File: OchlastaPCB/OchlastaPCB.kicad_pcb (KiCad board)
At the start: 4 copper layers, 175.1 x 89.9 mm, 37 parts, among them J1 XT60PW-M, J2 5V, U1 AP64501SP-13, U2 AP3429, U3 STM32F334R8Tx

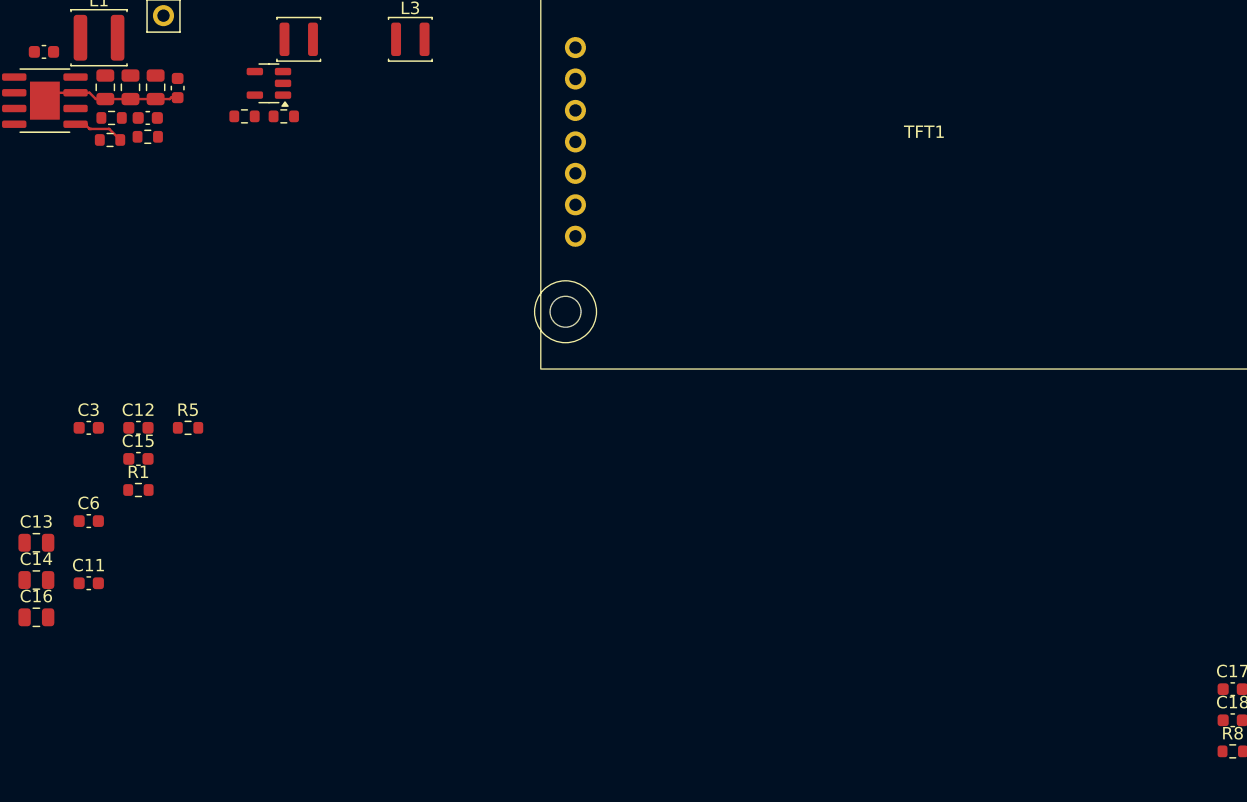
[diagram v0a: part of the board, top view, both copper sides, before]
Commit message: Precision LDO for analog circuitry in schematics
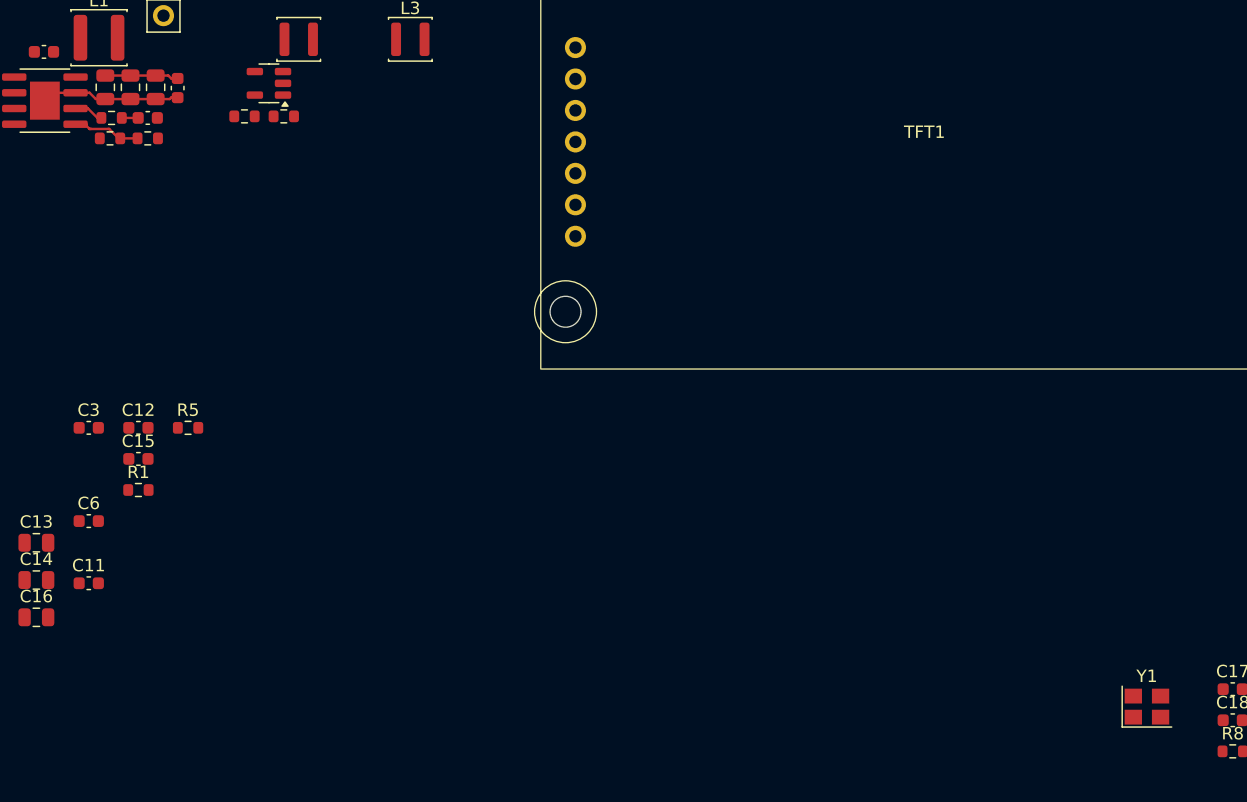
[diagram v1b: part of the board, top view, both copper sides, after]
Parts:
- added Y1: Crystal_GND24, Crystal:Crystal_SMD_3225-4Pin_3.2x2.5mm, F.Cu at (171.5, 94.0)
- moved R3 0.13 mm to (90.8, 48.1)
- moved R4 0.13 mm to (87.8, 48.1)
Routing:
- net 5V: track 0.00 -> 5.94 mm
- net Net-(U1-COMP): track 0.00 -> 2.40 mm
- net Net-(U1-FB): track 4.34 -> 5.74 mm
- net Net-(C5-Pad1): track 0.00 -> 1.32 mm

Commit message: Schematics seems finished, starting PCB design
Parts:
- added C19: 10n, Capacitor_SMD:C_0603_1608Metric, F.Cu at (395.9, 108.9)
- added C20: 100 nF, Capacitor_SMD:C_0603_1608Metric, F.Cu at (395.9, 111.4)
- added C21: 22 uF, Capacitor_SMD:C_0805_2012Metric, F.Cu at (485.3, 58.2)
- added C22: 100 n, Capacitor_SMD:C_0603_1608Metric, F.Cu at (395.9, 113.9)
- added C23: 100 n, Capacitor_SMD:C_0603_1608Metric, F.Cu at (395.9, 116.4)
- added C24: 100 n, Capacitor_SMD:C_0603_1608Metric, F.Cu at (399.9, 81.3)
- added C25: 100 n, Capacitor_SMD:C_0603_1608Metric, F.Cu at (399.9, 83.8)
- added C26: 100 n, Capacitor_SMD:C_0603_1608Metric, F.Cu at (399.9, 86.3)
- added C27: 100 n, Capacitor_SMD:C_0603_1608Metric, F.Cu at (399.9, 88.8)
- added C28: 100 n, Capacitor_SMD:C_0603_1608Metric, F.Cu at (399.9, 91.3)
- added C29: 10 uF 50V, Capacitor_SMD:C_1206_3216Metric, F.Cu at (85.0, 122.4)
- added C30: 10 uF 50V, Capacitor_SMD:C_1206_3216Metric, F.Cu at (85.0, 125.8)
- added C31: 10 nF, Capacitor_SMD:C_0603_1608Metric, F.Cu at (399.9, 93.8)
- added C32: 100 nF, Capacitor_SMD:C_0603_1608Metric, F.Cu at (399.9, 96.3)
- added C33: 2.7 nF, Capacitor_SMD:C_0603_1608Metric, F.Cu at (399.9, 98.8)
- added C34: open, Capacitor_SMD:C_0603_1608Metric, F.Cu at (399.9, 101.3)
- added C35: 100 nF, Capacitor_SMD:C_0603_1608Metric, F.Cu at (399.9, 103.9)
- added C36: 22 uF, Capacitor_SMD:C_0805_2012Metric, F.Cu at (485.3, 61.2)
- added C37: 22 uF, Capacitor_SMD:C_0805_2012Metric, F.Cu at (485.3, 64.2)
- added C38: 100 n, Capacitor_SMD:C_0603_1608Metric, F.Cu at (399.9, 106.4)
- added C39: 1 u, Capacitor_SMD:C_0603_1608Metric, F.Cu at (399.9, 108.9)
- added C40: 100 n, Capacitor_SMD:C_0603_1608Metric, F.Cu at (399.9, 111.4)
- added C41: 10 uF 50V, Capacitor_SMD:C_1206_3216Metric, F.Cu at (396.7, 169.3)
- added C42: 10 uF 50V, Capacitor_SMD:C_1206_3216Metric, F.Cu at (402.4, 155.9)
- added C43: 10 uF 50V, Capacitor_SMD:C_1206_3216Metric, F.Cu at (402.4, 159.2)
- added C44: 10 uF 50V, Capacitor_SMD:C_1206_3216Metric, F.Cu at (402.4, 162.6)
- added C45: 100 n, Capacitor_SMD:C_0603_1608Metric, F.Cu at (399.9, 113.9)
- added C46: 1 u, Capacitor_SMD:C_0603_1608Metric, F.Cu at (399.9, 116.4)
- added C47: 100 n, Capacitor_SMD:C_0603_1608Metric, F.Cu at (403.9, 81.3)
- added C48: 10 uF 50V, Capacitor_SMD:C_1206_3216Metric, F.Cu at (402.4, 165.9)
- added C49: 10 uF 50V, Capacitor_SMD:C_1206_3216Metric, F.Cu at (402.4, 169.3)
- added C50: 10 uF 50V, Capacitor_SMD:C_1206_3216Metric, F.Cu at (408.0, 155.9)
- added C51: 10 uF 50V, Capacitor_SMD:C_1206_3216Metric, F.Cu at (408.0, 159.2)
- added C52: 100 n, Capacitor_SMD:C_0603_1608Metric, F.Cu at (403.9, 83.8)
- added C53: 100 n, Capacitor_SMD:C_0603_1608Metric, F.Cu at (403.9, 86.3)
- added C54: 1 u, Capacitor_SMD:C_0603_1608Metric, F.Cu at (403.9, 88.8)
- added C55: 1 u, Capacitor_SMD:C_0603_1608Metric, F.Cu at (403.9, 91.3)
- added C56: 100 n, Capacitor_SMD:C_0603_1608Metric, F.Cu at (403.9, 93.8)
- added C57: 100 n, Capacitor_SMD:C_0603_1608Metric, F.Cu at (403.9, 96.3)
- added C58: 10 uF 50V, Capacitor_SMD:C_1206_3216Metric, F.Cu at (408.0, 162.6)
- added C59: 10 uF 50V, Capacitor_SMD:C_1206_3216Metric, F.Cu at (408.0, 165.9)
- added C60: 10 uF 50V, Capacitor_SMD:C_1206_3216Metric, F.Cu at (408.0, 169.3)
- added C61: 10 uF 50V, Capacitor_SMD:C_1206_3216Metric, F.Cu at (413.7, 155.9)
- added C62: 10 uF 50V, Capacitor_SMD:C_1206_3216Metric, F.Cu at (413.7, 159.2)
- added C63: 10 uF 50V, Capacitor_SMD:C_1206_3216Metric, F.Cu at (413.7, 162.6)
- added C64: 10 uF 50V, Capacitor_SMD:C_1206_3216Metric, F.Cu at (413.7, 165.9)
- added C65: 10 uF 50V, Capacitor_SMD:C_1206_3216Metric, F.Cu at (413.7, 169.3)
- added C66: 100 n, Capacitor_SMD:C_0603_1608Metric, F.Cu at (403.9, 98.8)
- added C67: 100 n, Capacitor_SMD:C_0603_1608Metric, F.Cu at (403.9, 101.3)
- added C68: 100 n, Capacitor_SMD:C_0603_1608Metric, F.Cu at (403.9, 103.9)
- added C69: 100 n, Capacitor_SMD:C_0603_1608Metric, F.Cu at (403.9, 106.4)
- added C70: 100 n, Capacitor_SMD:C_0603_1608Metric, F.Cu at (403.9, 108.9)
- added C71: 100 n, Capacitor_SMD:C_0603_1608Metric, F.Cu at (403.9, 111.4)
- added C72: 100 n, Capacitor_SMD:C_0603_1608Metric, F.Cu at (403.9, 113.9)
- added C73: 100 n, Capacitor_SMD:C_0603_1608Metric, F.Cu at (403.9, 116.4)
- added C74: 100 n, Capacitor_SMD:C_0603_1608Metric, F.Cu at (408.0, 81.3)
- added C75: 100 n, Capacitor_SMD:C_0603_1608Metric, F.Cu at (408.0, 83.8)
- added CP2: 100 uF, Capacitor_SMD:CP_Elec_8x10, F.Cu at (69.4, 57.4)
- added CP3: 100 uF, Capacitor_SMD:CP_Elec_8x10, F.Cu at (436.1, 120.9)
- added CP4: 100 uF, Capacitor_SMD:CP_Elec_8x10, F.Cu at (436.1, 130.8)
- added CP5: 100 uF, Capacitor_SMD:CP_Elec_8x10, F.Cu at (436.1, 140.6)
- added CP6: 100 uF, Capacitor_SMD:CP_Elec_8x10, F.Cu at (436.1, 150.5)
- added D1: SS14, Diode_SMD:D_SMA, F.Cu at (445.9, 98.6)
- added D10: SS14, Diode_SMD:D_SMA, F.Cu at (454.0, 112.2)
- added D11: SS14, Diode_SMD:D_SMA, F.Cu at (454.0, 116.8)
- added D12: SS14, Diode_SMD:D_SMA, F.Cu at (454.0, 121.3)
- added D13: SS14, Diode_SMD:D_SMA, F.Cu at (462.1, 98.6)
- added D14: SS14, Diode_SMD:D_SMA, F.Cu at (462.1, 103.1)
- added D15: SS14, Diode_SMD:D_SMA, F.Cu at (462.1, 107.7)
- added D16: SS14, Diode_SMD:D_SMA, F.Cu at (462.1, 112.2)
- added D2: SS14, Diode_SMD:D_SMA, F.Cu at (445.9, 103.1)
- added D3: SS14, Diode_SMD:D_SMA, F.Cu at (445.9, 107.7)
- added D4: SS14, Diode_SMD:D_SMA, F.Cu at (445.9, 112.2)
- added D5: SS14, Diode_SMD:D_SMA, F.Cu at (445.9, 116.8)
- added D6: SS14, Diode_SMD:D_SMA, F.Cu at (445.9, 121.3)
- added D7: SS14, Diode_SMD:D_SMA, F.Cu at (454.0, 98.6)
- added D8: SS14, Diode_SMD:D_SMA, F.Cu at (454.0, 103.1)
- added D9: SS14, Diode_SMD:D_SMA, F.Cu at (454.0, 107.7)
- added H1: MountingHole_Pad, MountingHole:MountingHole_3.2mm_M3_Pad_Via, F.Cu at (470.1, 45.6)
- added H2: MountingHole_Pad, MountingHole:MountingHole_3.2mm_M3_Pad_Via, F.Cu at (470.1, 53.6)
- added H3: MountingHole_Pad, MountingHole:MountingHole_3.2mm_M3_Pad_Via, F.Cu at (470.1, 61.5)
- added H4: MountingHole_Pad, MountingHole:MountingHole_3.2mm_M3_Pad_Via, F.Cu at (470.1, 69.5)
- added J10: CAN term jmp, Connector_PinHeader_2.54mm:PinHeader_1x02_P2.54mm_Vertical, F.Cu at (481.0, 69.8)
- added J3: Conn_01x02_Socket, TerminalBlock_WAGO:TerminalBlock_WAGO_236-402_1x02_P5.00mm_45Degree, F.Cu at (38.5, 76.3)
- added J4: Conn_01x02_Socket, TerminalBlock_WAGO:TerminalBlock_WAGO_236-402_1x02_P5.00mm_45Degree, F.Cu at (38.5, 90.0)
- added J5: Conn_01x02_Socket, TerminalBlock_WAGO:TerminalBlock_WAGO_236-402_1x02_P5.00mm_45Degree, F.Cu at (38.5, 103.7)
- added J6: Conn_01x02_Socket, TerminalBlock_WAGO:TerminalBlock_WAGO_236-402_1x02_P5.00mm_45Degree, F.Cu at (38.5, 117.5)
- added J7: Debug, Connector_IDC:IDC-Header_2x05_P2.54mm_Vertical, F.Cu at (121.9, 19.6)
- added J8: UART, Connector_PinHeader_2.54mm:PinHeader_1x03_P2.54mm_Vertical, F.Cu at (418.8, 165.4)
- added J9: CAN, Connector_Phoenix_MC:PhoenixContact_MC_1,5_2-G-3.81_1x02_P3.81mm_Horizontal, F.Cu at (97.4, 25.8)
- added L4: 3.6 uH, Inductor_SMD:L_Changjiang_FNR4030S, F.Cu at (457.0, 72.5)
- added L5: 22 uH, Inductor_SMD:L_APV_APH1770, F.Cu at (384.0, 108.2)
- added L6: 22 uH, Inductor_SMD:L_APV_APH1770, F.Cu at (384.0, 127.0)
- added L7: 22 uH, Inductor_SMD:L_APV_APH1770, F.Cu at (384.0, 145.8)
- added Q1: IRFH7440, SnapMagic_downloads:PQFN_5x6_FET, F.Cu at (446.3, 126.9)
- added Q2: IRFH7440, SnapMagic_downloads:PQFN_5x6_FET, F.Cu at (446.3, 133.6)
- added Q3: IRFH7440, SnapMagic_downloads:PQFN_5x6_FET, F.Cu at (446.3, 140.2)
- added Q4: IRFH7440, SnapMagic_downloads:PQFN_5x6_FET, F.Cu at (446.3, 146.9)
- added Q5: IRFH7440, SnapMagic_downloads:PQFN_5x6_FET, F.Cu at (446.3, 153.5)
- added Q6: IRFH7440, SnapMagic_downloads:PQFN_5x6_FET, F.Cu at (454.9, 126.9)
- added Q7: IRFH7440, SnapMagic_downloads:PQFN_5x6_FET, F.Cu at (454.9, 133.6)
- added Q8: IRFH7440, SnapMagic_downloads:PQFN_5x6_FET, F.Cu at (454.9, 140.2)
- added R10: 40 k 1%, Resistor_SMD:R_0603_1608Metric, F.Cu at (408.0, 108.9)
- added R11: 22.1 k 1%, Resistor_SMD:R_0603_1608Metric, F.Cu at (408.0, 111.4)
- added R12: 10 k, Resistor_SMD:R_0603_1608Metric, F.Cu at (408.0, 113.9)
- added R13: 15 k, Resistor_SMD:R_0603_1608Metric, F.Cu at (408.0, 116.4)
- added R14: 200k 1%, Resistor_SMD:R_0603_1608Metric, F.Cu at (412.0, 81.3)
- added R15: 22.1 k 1%, Resistor_SMD:R_0603_1608Metric, F.Cu at (412.0, 83.8)
- added R16: 10 R, Resistor_SMD:R_0603_1608Metric, F.Cu at (412.0, 86.3)
- added R17: 10 R, Resistor_SMD:R_0603_1608Metric, F.Cu at (412.0, 88.8)
- added R18: 10 R, Resistor_SMD:R_0603_1608Metric, F.Cu at (412.0, 91.3)
- added R19: 10 R, Resistor_SMD:R_0603_1608Metric, F.Cu at (412.0, 93.8)
- added R20: 10 R, Resistor_SMD:R_0603_1608Metric, F.Cu at (412.0, 96.3)
- added R21: 10 R, Resistor_SMD:R_0603_1608Metric, F.Cu at (412.0, 98.8)
- added R22: 10 R, Resistor_SMD:R_0603_1608Metric, F.Cu at (412.0, 101.3)
- added R23: 10 R, Resistor_SMD:R_0603_1608Metric, F.Cu at (412.0, 103.9)
- added R24: 10 R, Resistor_SMD:R_0603_1608Metric, F.Cu at (412.0, 106.4)
- added R25: 10 R, Resistor_SMD:R_0603_1608Metric, F.Cu at (412.0, 108.9)
- added R26: 10 R, Resistor_SMD:R_0603_1608Metric, F.Cu at (412.0, 111.4)
- added R27: 10 R, Resistor_SMD:R_0603_1608Metric, F.Cu at (412.0, 113.9)
- added R28: 10 R, Resistor_SMD:R_0603_1608Metric, F.Cu at (412.0, 116.4)
- added R29: 10 R, Resistor_SMD:R_0603_1608Metric, F.Cu at (416.0, 81.3)
- added R30: 10 R, Resistor_SMD:R_0603_1608Metric, F.Cu at (416.0, 83.8)
- added R31: 10 R, Resistor_SMD:R_0603_1608Metric, F.Cu at (416.0, 86.3)
- added R32: 10k, Resistor_SMD:R_0603_1608Metric, F.Cu at (416.0, 88.8)
- added R33: 10k, Resistor_SMD:R_0603_1608Metric, F.Cu at (416.0, 91.3)
- added R34: 200k 1%, Resistor_SMD:R_0603_1608Metric, F.Cu at (59.2, 71.1)
- added R35: 22.1 k 1%, Resistor_SMD:R_0603_1608Metric, F.Cu at (416.0, 96.3)
- added R36: 200k 1%, Resistor_SMD:R_0603_1608Metric, F.Cu at (416.0, 98.8)
- added R37: 22.1 k 1%, Resistor_SMD:R_0603_1608Metric, F.Cu at (416.0, 101.3)
- added R38: 200k 1%, Resistor_SMD:R_0603_1608Metric, F.Cu at (416.0, 103.9)
- added R39: 22.1 k 1%, Resistor_SMD:R_0603_1608Metric, F.Cu at (416.0, 106.4)
- added R40: 200k 1%, Resistor_SMD:R_0603_1608Metric, F.Cu at (416.0, 108.9)
- added R41: 22.1 k 1%, Resistor_SMD:R_0603_1608Metric, F.Cu at (416.0, 111.4)
- added R42: 200k 1%, Resistor_SMD:R_0603_1608Metric, F.Cu at (416.0, 113.9)
- added R43: 22.1 k 1%, Resistor_SMD:R_0603_1608Metric, F.Cu at (416.0, 116.4)
- added R44: 120 R, Resistor_SMD:R_0603_1608Metric, F.Cu at (420.0, 81.3)
- added R45: 120 R / DNP, Resistor_SMD:R_0603_1608Metric, F.Cu at (420.0, 83.8)
- added R46: DNP / 120 R, Resistor_SMD:R_0603_1608Metric, F.Cu at (420.0, 86.3)
- added R47: 10 k, Resistor_SMD:R_0603_1608Metric, F.Cu at (420.0, 88.8)
- added R48: 10 k, Resistor_SMD:R_0603_1608Metric, F.Cu at (420.0, 91.3)
- added R49: 10 k, Resistor_SMD:R_0603_1608Metric, F.Cu at (420.0, 93.8)
- added R50: 10 k, Resistor_SMD:R_0603_1608Metric, F.Cu at (420.0, 96.3)
- added R51: 10 k, Resistor_SMD:R_0603_1608Metric, F.Cu at (420.0, 98.8)
- added R52: 10 k, Resistor_SMD:R_0603_1608Metric, F.Cu at (420.0, 101.3)
- added R53: 10 k, Resistor_SMD:R_0603_1608Metric, F.Cu at (420.0, 103.9)
- added R54: 10 k, Resistor_SMD:R_0603_1608Metric, F.Cu at (420.0, 106.4)
- added R55: 10 k, Resistor_SMD:R_0603_1608Metric, F.Cu at (420.0, 108.9)
- added R9: 10 k, Resistor_SMD:R_0603_1608Metric, F.Cu at (408.0, 106.4)
- added Ra1: 22.1 k 1%, Resistor_SMD:R_0603_1608Metric, F.Cu at (420.0, 111.4)
- added Ra2: 22.1 k 1%, Resistor_SMD:R_0603_1608Metric, F.Cu at (420.0, 113.9)
- added Ra3: 22.1 k 1%, Resistor_SMD:R_0603_1608Metric, F.Cu at (420.0, 116.4)
- added Ra4: 22.1 k 1%, Resistor_SMD:R_0603_1608Metric, F.Cu at (424.0, 81.3)
- added Ra5: 22.1 k 1%, Resistor_SMD:R_0603_1608Metric, F.Cu at (424.0, 83.8)
- added Ra6: 22.1 k 1%, Resistor_SMD:R_0603_1608Metric, F.Cu at (424.0, 86.3)
- added Ra7: 22.1 k 1%, Resistor_SMD:R_0603_1608Metric, F.Cu at (424.0, 88.8)
- added Ra8: 22.1 k 1%, Resistor_SMD:R_0603_1608Metric, F.Cu at (424.0, 91.3)
- added Rb1: 22.1 k 1%, Resistor_SMD:R_0603_1608Metric, F.Cu at (424.0, 93.8)
- added Rb2: 22.1 k 1%, Resistor_SMD:R_0603_1608Metric, F.Cu at (424.0, 96.3)
- added Rb3: 22.1 k 1%, Resistor_SMD:R_0603_1608Metric, F.Cu at (424.0, 98.8)
- added Rb4: 22.1 k 1%, Resistor_SMD:R_0603_1608Metric, F.Cu at (424.0, 101.3)
- added Rb5: 22.1 k 1%, Resistor_SMD:R_0603_1608Metric, F.Cu at (424.0, 103.9)
- added Rb6: 22.1 k 1%, Resistor_SMD:R_0603_1608Metric, F.Cu at (424.0, 106.4)
- added Rb7: 22.1 k 1%, Resistor_SMD:R_0603_1608Metric, F.Cu at (424.0, 108.9)
- added Rb8: 22.1 k 1%, Resistor_SMD:R_0603_1608Metric, F.Cu at (424.0, 111.4)
- added Rc1: 820 R, Resistor_SMD:R_0603_1608Metric, F.Cu at (424.0, 113.9)
- added Rc2: 820 R, Resistor_SMD:R_0603_1608Metric, F.Cu at (424.0, 116.4)
- added Rc3: 820 R, Resistor_SMD:R_0603_1608Metric, F.Cu at (428.0, 81.3)
- added Rc4: 820 R, Resistor_SMD:R_0603_1608Metric, F.Cu at (428.0, 83.8)
- added Rc5: 820 R, Resistor_SMD:R_0603_1608Metric, F.Cu at (428.0, 86.3)
- added Rc6: 820 R, Resistor_SMD:R_0603_1608Metric, F.Cu at (428.0, 88.8)
- added Rc7: 820 R, Resistor_SMD:R_0603_1608Metric, F.Cu at (428.0, 91.3)
- added Rc8: 820 R, Resistor_SMD:R_0603_1608Metric, F.Cu at (428.0, 93.8)
- added Rg1: 2.7 k 1%, Resistor_SMD:R_0603_1608Metric, F.Cu at (428.0, 96.3)
- added Rg2: 2.7 k 1%, Resistor_SMD:R_0603_1608Metric, F.Cu at (428.0, 98.8)
- added Rg3: 2.7 k 1%, Resistor_SMD:R_0603_1608Metric, F.Cu at (428.0, 101.3)
- added Rg4: 2.7 k 1%, Resistor_SMD:R_0603_1608Metric, F.Cu at (428.0, 103.9)
- added Rg5: 2.7 k 1%, Resistor_SMD:R_0603_1608Metric, F.Cu at (428.0, 106.4)
- added Rg6: 2.7 k 1%, Resistor_SMD:R_0603_1608Metric, F.Cu at (428.0, 108.9)
- added Rg7: 2.7 k 1%, Resistor_SMD:R_0603_1608Metric, F.Cu at (428.0, 111.4)
- added Rg8: 2.7 k 1%, Resistor_SMD:R_0603_1608Metric, F.Cu at (428.0, 113.9)
- added Rshunt1: 5 mR, Resistor_SMD:R_1206_3216Metric, F.Cu at (64.5, 80.3)
- added Rshunt2: 5 mR, Resistor_SMD:R_1206_3216Metric, F.Cu at (481.7, 166.1)
- added Rshunt3: 5 mR, Resistor_SMD:R_1206_3216Metric, F.Cu at (481.7, 169.4)
- added Rshunt4: 5 mR, Resistor_SMD:R_1206_3216Metric, F.Cu at (481.7, 172.7)
- added SW1: SW_RESET, OchlastaFootprints:SW_Push_SPST_CheapAtJLC, F.Cu at (419.8, 156.4)
- added SW2: SW_BOOT, OchlastaFootprints:SW_Push_SPST_CheapAtJLC, F.Cu at (419.8, 160.9)
- added SW3: BTN_A, Button_Switch_THT:SW_PUSH_6mm, F.Cu at (461.0, 125.6)
- added SW4: RotaryEncoder_Switch, Rotary_Encoder:RotaryEncoder_Alps_EC11E-Switch_Vertical_H20mm, F.Cu at (468.1, 101.4)
- added SW5: BTN_B, Button_Switch_THT:SW_PUSH_6mm, F.Cu at (461.0, 134.2)
- added SW6: BTN_C, Button_Switch_THT:SW_PUSH_6mm, F.Cu at (461.0, 142.7)
- added SW7: BTN_D, Button_Switch_THT:SW_PUSH_6mm, F.Cu at (461.0, 151.3)
- added SW8: BTN_L, Button_Switch_THT:SW_PUSH_6mm, F.Cu at (461.0, 159.8)
- added SW9: BTN_R, Button_Switch_THT:SW_PUSH_6mm, F.Cu at (461.0, 168.4)
- added TH1: PT1000, Connector_Phoenix_MC:PhoenixContact_MC_1,5_2-G-3.81_1x02_P3.81mm_Horizontal, F.Cu at (223.1, 53.7)
- added TH2: PT1000, Connector_Phoenix_MC:PhoenixContact_MC_1,5_2-G-3.81_1x02_P3.81mm_Horizontal, F.Cu at (223.1, 63.8)
- added TH3: PT1000, Connector_Phoenix_MC:PhoenixContact_MC_1,5_2-G-3.81_1x02_P3.81mm_Horizontal, F.Cu at (223.1, 74.0)
- added TH4: PT1000, Connector_Phoenix_MC:PhoenixContact_MC_1,5_2-G-3.81_1x02_P3.81mm_Horizontal, F.Cu at (223.1, 84.1)
- added TH5: PT1000, Connector_Phoenix_MC:PhoenixContact_MC_1,5_2-G-3.81_1x02_P3.81mm_Horizontal, F.Cu at (223.1, 94.3)
- added TH6: PT1000, Connector_Phoenix_MC:PhoenixContact_MC_1,5_2-G-3.81_1x02_P3.81mm_Horizontal, F.Cu at (223.1, 104.5)
- added TH7: PT1000, Connector_Phoenix_MC:PhoenixContact_MC_1,5_2-G-3.81_1x02_P3.81mm_Horizontal, F.Cu at (223.1, 114.6)
- added TH8: PT1000, Connector_Phoenix_MC:PhoenixContact_MC_1,5_2-G-3.81_1x02_P3.81mm_Horizontal, F.Cu at (223.1, 124.8)
- added U10: INA333xxDGK, Package_SO:VSSOP-8_3x3mm_P0.65mm, F.Cu at (450.4, 67.3)
- added U11: INA333xxDGK, Package_SO:VSSOP-8_3x3mm_P0.65mm, F.Cu at (450.4, 71.9)
- added U12: INA333xxDGK, Package_SO:VSSOP-8_3x3mm_P0.65mm, F.Cu at (450.4, 76.6)
- added U13: UCC27282DR, SnapMagic_downloads:SOIC127P599X175-8N, F.Cu at (478.9, 44.9)
- added U14: AP64501SP-13, SnapMagic_downloads:SOIC127P600X170-9N, F.Cu at (474.7, 171.2)
- added U15: UCC27282DR, SnapMagic_downloads:SOIC127P599X175-8N, F.Cu at (478.9, 51.3)
- added U16: UCC27282DR, SnapMagic_downloads:SOIC127P599X175-8N, F.Cu at (478.9, 57.8)
- added U17: UCC27282DR, SnapMagic_downloads:SOIC127P599X175-8N, F.Cu at (478.9, 64.3)
- added U18: INA240A2D, Package_SO:SOIC-8_3.9x4.9mm_P1.27mm, F.Cu at (444.3, 162.8)
- added U19: INA240A2D, Package_SO:SOIC-8_3.9x4.9mm_P1.27mm, F.Cu at (442.5, 51.6)
- added U20: INA240A2D, Package_SO:SOIC-8_3.9x4.9mm_P1.27mm, F.Cu at (442.5, 58.2)
- added U21: INA240A2D, Package_SO:SOIC-8_3.9x4.9mm_P1.27mm, F.Cu at (442.5, 64.8)
- added U22: SN65HVD230, Package_SO:SOIC-8_3.9x4.9mm_P1.27mm, F.Cu at (442.5, 71.3)
- added U4: INA333xxDGK, Package_SO:VSSOP-8_3x3mm_P0.65mm, F.Cu at (450.4, 44.0)
- added U5: TPS7A4901DGNR_Trafo_Edit, SnapMagic_downloads:SOP65P490X110-9N, F.Cu at (425.5, 165.4)
- added U6: INA333xxDGK, Package_SO:VSSOP-8_3x3mm_P0.65mm, F.Cu at (450.4, 48.7)
- added U7: INA333xxDGK, Package_SO:VSSOP-8_3x3mm_P0.65mm, F.Cu at (450.4, 53.3)
- added U8: INA333xxDGK, Package_SO:VSSOP-8_3x3mm_P0.65mm, F.Cu at (450.4, 58.0)
- added U9: INA333xxDGK, Package_SO:VSSOP-8_3x3mm_P0.65mm, F.Cu at (450.4, 62.6)
- C15: value 100 nF -> 100 n
- C16: value 22 uF -> 10n; footprint Capacitor_SMD:C_0805_2012Metric -> Capacitor_SMD:C_0603_1608Metric
- L3: value 2.2 uH -> 22 uH; footprint Inductor_SMD:L_Changjiang_FNR3015S -> Inductor_SMD:L_APV_APH1770
- moved C16 314.5 mm to (395.9, 101.3)
- moved C15 306.9 mm to (395.9, 98.8)
- moved U3 295.2 mm to (476.8, 154.0)
- moved L3 276.5 mm to (384.0, 89.4)
- moved Y1 261.8 mm to (425.7, 156.4)
- moved R8 229.6 mm to (408.0, 103.9)
- moved C17 217.8 mm to (395.9, 103.9)
- moved C18 217.8 mm to (395.9, 106.4)
- moved TFT1 201.8 mm to (218.9, -142.7)
- moved C11 60.9 mm to (141.1, 58.0)
- moved R5 60.0 mm to (153.1, 60.5)
- moved R7 57.7 mm to (153.1, 65.5), turned to 0 degrees
- moved R6 53.9 mm to (153.1, 63.0)
- moved C13 53.8 mm to (130.4, 57.7)
- moved C14 53.8 mm to (130.4, 60.7)
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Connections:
- net 5V renamed +5V
- C16 pad 1: +3.3VA -> Net-(U5-FB)
- C17 pad 1: Net-(C17-Pad1) -> /HSE_OUT
- L3 pad 1: +3V3 -> Net-(D2-A)
- L3 pad 2: +3.3VA -> Net-(U18-+)
- R8 pad 1: unconnected-(R8-Pad1) -> /HSE_IN
- TFT1 pad 3: unconnected-(TFT1-SCL-Pad3) -> /SPI_SCK
- TFT1 pad 4: unconnected-(TFT1-SDA/MOSI-Pad4) -> /SPI_MOSI
- TFT1 pad 5: unconnected-(TFT1-RST-Pad5) -> /PB10_Disp_RST
- TFT1 pad 6: unconnected-(TFT1-DC-Pad6) -> /PB11_Disp_DC
- TFT1 pad 7: unconnected-(TFT1-CS-Pad7) -> /PB9_Disp_CS
- U3 pad 1: unconnected-(U3-VBAT-Pad1) -> +3V3
- U3 pad 10: unconnected-(U3-PC2-Pad10) -> /U_out_3
- U3 pad 11: unconnected-(U3-PC3-Pad11) -> /temp_U_out_1
- U3 pad 12: unconnected-(U3-VSSA-Pad12) -> GND
- U3 pad 13: unconnected-(U3-VDDA-Pad13) -> +3.3VA
- U3 pad 14: unconnected-(U3-PA0-Pad14) -> /I_out_1
- U3 pad 15: unconnected-(U3-PA1-Pad15) -> /I_out_2
- U3 pad 16: unconnected-(U3-PA2-Pad16) -> /I_out_3
- U3 pad 17: unconnected-(U3-PA3-Pad17) -> /I_out_4
- U3 pad 18: Net-(U3-VSS-Pad18) -> GND
- U3 pad 19: unconnected-(U3-VDD-Pad19) -> +3V3
- U3 pad 2: unconnected-(U3-PC13-Pad2) -> /BTN_L
- U3 pad 20: unconnected-(U3-PA4-Pad20) -> /temp_U_out_2
- U3 pad 21: unconnected-(U3-PA5-Pad21) -> /temp_U_out_3
- U3 pad 22: unconnected-(U3-PA6-Pad22) -> /temp_U_out_4
- U3 pad 23: unconnected-(U3-PA7-Pad23) -> /temp_U_out_5
- U3 pad 24: unconnected-(U3-PC4-Pad24) -> /temp_U_out_6
- U3 pad 25: unconnected-(U3-PC5-Pad25) -> /temp_U_out_7
- U3 pad 26: unconnected-(U3-PB0-Pad26) -> /U_out_4
- U3 pad 27: unconnected-(U3-PB1-Pad27) -> /U_input_div
- U3 pad 28: unconnected-(U3-PB2-Pad28) -> /temp_U_out_8
- U3 pad 29: unconnected-(U3-PB10-Pad29) -> /PB10_Disp_RST
- U3 pad 3: unconnected-(U3-PC14-Pad3) -> /BTN_R
- U3 pad 30: unconnected-(U3-PB11-Pad30) -> /PB11_Disp_DC
- U3 pad 31: Net-(U3-VSS-Pad18) -> GND
- U3 pad 32: unconnected-(U3-VDD-Pad32) -> +3V3
- U3 pad 33: unconnected-(U3-PB12-Pad33) -> /HRTIM_C_Hi
- U3 pad 34: unconnected-(U3-PB13-Pad34) -> /HRTIM_C_Lo
- U3 pad 35: unconnected-(U3-PB14-Pad35) -> /HRTIM_D_Hi
- U3 pad 36: unconnected-(U3-PB15-Pad36) -> /HRTIM_D_Lo
- U3 pad 37: unconnected-(U3-PC6-Pad37) -> /ENC_A
- U3 pad 38: unconnected-(U3-PC7-Pad38) -> /ENC_B
- U3 pad 39: unconnected-(U3-PC8-Pad39) -> /BTN_ENC
- U3 pad 40: unconnected-(U3-PC9-Pad40) -> /BTN_A
- U3 pad 41: unconnected-(U3-PA8-Pad41) -> /HRTIM_A_Hi
- U3 pad 42: unconnected-(U3-PA9-Pad42) -> /HRTIM_A_Lo
- U3 pad 43: unconnected-(U3-PA10-Pad43) -> /HRTIM_B_Hi
- U3 pad 44: unconnected-(U3-PA11-Pad44) -> /HRTIM_B_Lo
- U3 pad 45: unconnected-(U3-PA12-Pad45) -> /CAN_TX
- U3 pad 46: unconnected-(U3-PA13-Pad46) -> /SWDIO
- U3 pad 47: Net-(U3-VSS-Pad18) -> GND
- U3 pad 48: unconnected-(U3-VDD-Pad48) -> +3V3
- U3 pad 49: unconnected-(U3-PA14-Pad49) -> /SWCLK
- U3 pad 5: unconnected-(U3-PF0-Pad5) -> /HSE_IN
- U3 pad 51: unconnected-(U3-PC10-Pad51) -> /BTN_B
- U3 pad 52: unconnected-(U3-PC11-Pad52) -> /BTN_C
- U3 pad 53: unconnected-(U3-PC12-Pad53) -> /BTN_D
- U3 pad 55: unconnected-(U3-PB3-Pad55) -> /SPI_SCK
- U3 pad 56: unconnected-(U3-PB4-Pad56) -> /SPI_MISO
- U3 pad 57: unconnected-(U3-PB5-Pad57) -> /SPI_MOSI
- U3 pad 58: unconnected-(U3-PB6-Pad58) -> /UART_TX
- U3 pad 59: unconnected-(U3-PB7-Pad59) -> /UART_RX
- U3 pad 6: unconnected-(U3-PF1-Pad6) -> /HSE_OUT
- U3 pad 60: unconnected-(U3-BOOT0-Pad60) -> /BOOT0
- U3 pad 61: unconnected-(U3-PB8-Pad61) -> /CAN_RX
- U3 pad 62: unconnected-(U3-PB9-Pad62) -> /PB9_Disp_CS
- U3 pad 63: Net-(U3-VSS-Pad18) -> GND
- U3 pad 64: unconnected-(U3-VDD-Pad64) -> +3V3
- U3 pad 7: unconnected-(U3-NRST-Pad7) -> /NRST
- U3 pad 8: unconnected-(U3-PC0-Pad8) -> /U_out_1
- U3 pad 9: unconnected-(U3-PC1-Pad9) -> /U_out_2
- Y1 pad 1: Net-(C17-Pad1) -> /HSE_OUT
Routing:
- net GND: track 11.3 -> 0.00 mm
- net +5V: track 5.94 -> 0.00 mm
- net Net-(U1-COMP): track 2.40 -> 0.00 mm
- net Net-(U1-SW): track 0.00 -> 2.38 mm
- net Net-(U1-BST): track 0.00 -> 2.38 mm
- net Net-(C5-Pad1): track 1.32 -> 0.00 mm
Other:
- board size 175.1 x 89.9 mm -> 60.5 x 30.5 mm
